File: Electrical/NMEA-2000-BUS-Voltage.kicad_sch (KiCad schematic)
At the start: 6 parts, among them SW1 SW_Push, U1 WeMos_D1_mini

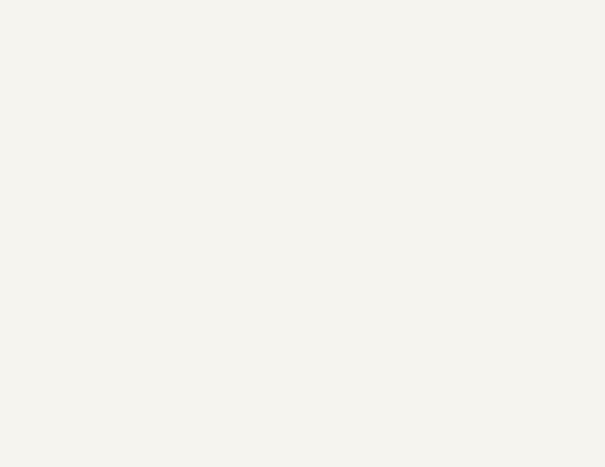
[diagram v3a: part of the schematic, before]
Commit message: Added LM7805
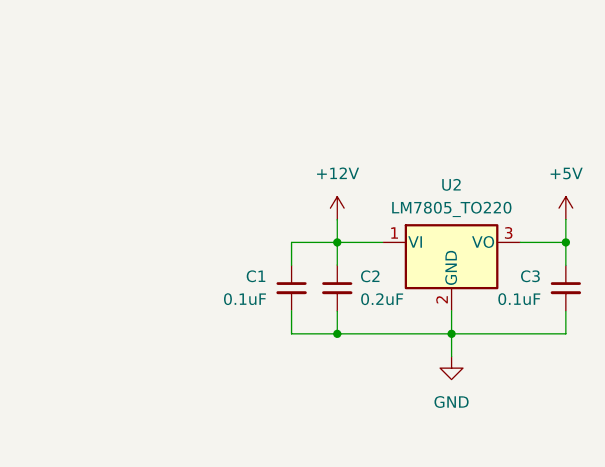
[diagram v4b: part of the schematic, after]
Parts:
- added C1, C3: 0.1uF, symbol Device:C_Small
- added C2: 0.2uF, symbol Device:C_Small
- added U2: LM7805_TO220, Package_TO_SOT_THT:TO-220-3_Vertical, symbol Regulator_Linear:LM7805_TO220
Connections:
- net +12V: now also C1.1, C2.1, U2.1 (VI)
- net +5V: now also C3.1, U2.3 (VO)
- net GND: now also C1.2, C2.2, C3.2, U2.2 (GND)
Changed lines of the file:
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@@
 (kicad_sch (version 20230121) (generator eeschema)
   (paper "A4")
+  (junction (at 168.91 114.3) (diameter 0) (color 0 0 0 0)
+  )
+  (junction (at 181.61 114.3) (diameter 0) (color 0 0 0 0)
+  )
+  (junction (at 168.91 104.14) (diameter 0) (color 0 0 0 0)
+  )
+  (junction (at 194.31 104.14) (diameter 0) (color 0 0 0 0)
+  )
   (junction (at 96.52 80.01) (diameter 0) (color 0 0 0 0)
   )
@@
     (stroke (width 0) (type default))
   )
+  (wire (pts (xy 168.91 101.6) (xy 168.91 104.14))
+    (stroke (width 0) (type default))
+  )
+  (wire (pts (xy 163.83 104.14) (xy 163.83 106.68))
+    (stroke (width 0) (type default))
+  )
+  (wire (pts (xy 168.91 104.14) (xy 163.83 104.14))
+    (stroke (width 0) (type default))
+  )
   (wire (pts (xy 46.99 74.93) (xy 46.99 77.47))
     (stroke (width 0) (type default))
   )
+  (wire (pts (xy 194.31 104.14) (xy 194.31 106.68))
+    (stroke (width 0) (type default))
+  )
   (wire (pts (xy 96.52 110.49) (xy 96.52 113.03))
     (stroke (width 0) (type default))
@@
     (stroke (width 0) (type default))
   )
+  (wire (pts (xy 168.91 114.3) (xy 181.61 114.3))
+    (stroke (width 0) (type default))
+  )
   (wire (pts (xy 64.77 92.71) (xy 59.69 92.71))
     (stroke (width 0) (type default))
@@
     (stroke (width 0) (type default))
   )
+  (wire (pts (xy 168.91 111.76) (xy 168.91 114.3))
+    (stroke (width 0) (type default))
+  )
+  (wire (pts (xy 194.31 114.3) (xy 194.31 111.76))
+    (stroke (width 0) (type default))
+  )
   (wire (pts (xy 59.69 95.25) (xy 64.77 95.25))
     (stroke (width 0) (type default))
@@
     (stroke (width 0) (type default))
   )
+  (wire (pts (xy 181.61 114.3) (xy 194.31 114.3))
+    (stroke (width 0) (type default))
+  )
+  (wire (pts (xy 189.23 104.14) (xy 194.31 104.14))
+    (stroke (width 0) (type default))
+  )
+  (wire (pts (xy 181.61 111.76) (xy 181.61 114.3))
+    (stroke (width 0) (type default))
+  )
+  (wire (pts (xy 168.91 104.14) (xy 173.99 104.14))
+    (stroke (width 0) (type default))
+  )
   (wire (pts (xy 59.69 85.09) (xy 64.77 85.09))
     (stroke (width 0) (type default))
@@
     (stroke (width 0) (type default))
   )
+  (wire (pts (xy 163.83 111.76) (xy 163.83 114.3))
+    (stroke (width 0) (type default))
+  )
   (wire (pts (xy 34.29 95.25) (xy 39.37 95.25))
     (stroke (width 0) (type default))
   )
+  (wire (pts (xy 168.91 104.14) (xy 168.91 106.68))
+    (stroke (width 0) (type default))
+  )
+  (wire (pts (xy 181.61 114.3) (xy 181.61 116.84))
+    (stroke (width 0) (type default))
+  )
   (wire (pts (xy 64.77 107.95) (xy 59.69 107.95))
     (stroke (width 0) (type default))
   )
   (wire (pts (xy 124.46 74.93) (xy 124.46 77.47))
+    (stroke (width 0) (type default))
+  )
+  (wire (pts (xy 194.31 101.6) (xy 194.31 104.14))
+    (stroke (width 0) (type default))
+  )
+  (wire (pts (xy 163.83 114.3) (xy 168.91 114.3))
     (stroke (width 0) (type default))
   )
@@
   (label "D1" (at 64.77 90.17 180) (fields_autoplaced)
     (effects (font (size 1.27 1.27)) (justify right bottom))
+  )
+  (symbol (lib_id "Device:C_Small") (at 163.83 109.22 0) (unit 1)
+    (in_bom yes) (on_board yes) (dnp no)
+    (property "Reference" "C1" (at 158.75 107.95 0)
+      (effects (font (size 1.27 1.27)) (justify left))
+    )
+    (property "Value" "0.1uF" (at 156.21 110.49 0)
+      (effects (font (size 1.27 1.27)) (justify left))
+    )
+    (property "Footprint" "" (at 163.83 109.22 0)
+      (effects (font (size 1.27 1.27)) hide)
+    )
+    (property "Datasheet" "~" (at 163.83 109.22 0)
+      (effects (font (size 1.27 1.27)) hide)
+    )
+    (pin "1")
+    (pin "2")
+    (instances
+      (project "NMEA-2000-BUS-Voltage"
+        (path "/2ad9a196-bb2f-4407-b356-e110a1476183"
+          (reference "C1") (unit 1)
+        )
+      )
+    )
   )
   (symbol (lib_id "MCU_Module:WeMos_D1_mini") (at 49.53 97.79 0) (unit 1)
@@
     )
   )
+  (symbol (lib_id "power:+12V") (at 168.91 101.6 0) (unit 1)
+    (in_bom yes) (on_board yes) (dnp no) (fields_autoplaced)
+    (property "Reference" "#PWR07" (at 168.91 105.41 0)
+      (effects (font (size 1.27 1.27)) hide)
+    )
+    (property "Value" "+12V" (at 168.91 96.52 0)
+      (effects (font (size 1.27 1.27)))
+    )
+    (property "Footprint" "" (at 168.91 101.6 0)
+      (effects (font (size 1.27 1.27)) hide)
+    )
+    (property "Datasheet" "" (at 168.91 101.6 0)
+      (effects (font (size 1.27 1.27)) hide)
+    )
+    (pin "1")
+    (instances
+      (project "NMEA-2000-BUS-Voltage"
+        (path "/2ad9a196-bb2f-4407-b356-e110a1476183"
+          (reference "#PWR07") (unit 1)
+        )
+      )
+    )
+  )
   (symbol (lib_id "power:GND") (at 96.52 113.03 0) (unit 1)
     (in_bom yes) (on_board yes) (dnp no) (fields_autoplaced)
@@
     )
   )
+  (symbol (lib_id "power:GND") (at 181.61 116.84 0) (unit 1)
+    (in_bom yes) (on_board yes) (dnp no) (fields_autoplaced)
+    (property "Reference" "#PWR08" (at 181.61 123.19 0)
+      (effects (font (size 1.27 1.27)) hide)
+    )
+    (property "Value" "GND" (at 181.61 121.92 0)
+      (effects (font (size 1.27 1.27)))
+    )
+    (property "Footprint" "" (at 181.61 116.84 0)
+      (effects (font (size 1.27 1.27)) hide)
+    )
+    (property "Datasheet" "" (at 181.61 116.84 0)
+      (effects (font (size 1.27 1.27)) hide)
+    )
+    (pin "1")
+    (instances
+      (project "NMEA-2000-BUS-Voltage"
+        (path "/2ad9a196-bb2f-4407-b356-e110a1476183"
+          (reference "#PWR08") (unit 1)
+        )
+      )
+    )
+  )
   (symbol (lib_id "power:GND") (at 124.46 77.47 0) (unit 1)
     (in_bom yes) (on_board yes) (dnp no) (fields_autoplaced)
@@
     )
   )
+  (symbol (lib_id "Device:C_Small") (at 194.31 109.22 0) (unit 1)
+    (in_bom yes) (on_board yes) (dnp no)
+    (property "Reference" "C3" (at 189.23 107.95 0)
+      (effects (font (size 1.27 1.27)) (justify left))
+    )
+    (property "Value" "0.1uF" (at 186.69 110.49 0)
+      (effects (font (size 1.27 1.27)) (justify left))
+    )
+    (property "Footprint" "" (at 194.31 109.22 0)
+      (effects (font (size 1.27 1.27)) hide)
+    )
+    (property "Datasheet" "~" (at 194.31 109.22 0)
+      (effects (font (size 1.27 1.27)) hide)
+    )
+    (pin "1")
+    (pin "2")
+    (instances
+      (project "NMEA-2000-BUS-Voltage"
+        (path "/2ad9a196-bb2f-4407-b356-e110a1476183"
+          (reference "C3") (unit 1)
+        )
+      )
+    )
+  )
+  (symbol (lib_id "Device:C_Small") (at 168.91 109.22 0) (unit 1)
+    (in_bom yes) (on_board yes) (dnp no) (fields_autoplaced)
+    (property "Reference" "C2" (at 171.45 107.9563 0)
+      (effects (font (size 1.27 1.27)) (justify left))
+    )
+    (property "Value" "0.2uF" (at 171.45 110.4963 0)
+      (effects (font (size 1.27 1.27)) (justify left))
+    )
+    (property "Footprint" "" (at 168.91 109.22 0)
+      (effects (font (size 1.27 1.27)) hide)
+    )
+    (property "Datasheet" "~" (at 168.91 109.22 0)
+      (effects (font (size 1.27 1.27)) hide)
+    )
+    (pin "1")
+    (pin "2")
+    (instances
+      (project "NMEA-2000-BUS-Voltage"
+        (path "/2ad9a196-bb2f-4407-b356-e110a1476183"
+          (reference "C2") (unit 1)
+        )
+      )
+    )
+  )
   (symbol (lib_id "Device:R") (at 96.52 96.52 0) (unit 1)
     (in_bom yes) (on_board yes) (dnp no) (fields_autoplaced)
@@
     )
   )
+  (symbol (lib_id "power:+5V") (at 194.31 101.6 0) (unit 1)
+    (in_bom yes) (on_board yes) (dnp no) (fields_autoplaced)
+    (property "Reference" "#PWR09" (at 194.31 105.41 0)
+      (effects (font (size 1.27 1.27)) hide)
+    )
+    (property "Value" "+5V" (at 194.31 96.52 0)
+      (effects (font (size 1.27 1.27)))
+    )
+    (property "Footprint" "" (at 194.31 101.6 0)
+      (effects (font (size 1.27 1.27)) hide)
+    )
+    (property "Datasheet" "" (at 194.31 101.6 0)
+      (effects (font (size 1.27 1.27)) hide)
+    )
+    (pin "1")
+    (instances
+      (project "NMEA-2000-BUS-Voltage"
+        (path "/2ad9a196-bb2f-4407-b356-e110a1476183"
+          (reference "#PWR09") (unit 1)
+        )
+      )
+    )
+  )
   (symbol (lib_id "power:+12V") (at 96.52 67.31 0) (unit 1)
     (in_bom yes) (on_board yes) (dnp no) (fields_autoplaced)
@@
         )
       )
+    )
+  )
+  (symbol (lib_id "Regulator_Linear:LM7805_TO220") (at 181.61 104.14 0) (unit 1)
+    (in_bom yes) (on_board yes) (dnp no) (fields_autoplaced)
+    (property "Reference" "U2" (at 181.61 97.79 0)
+      (effects (font (size 1.27 1.27)))
+    )
+    (property "Value" "LM7805_TO220" (at 181.61 100.33 0)
+      (effects (font (size 1.27 1.27)))
+    )
+    (property "Footprint" "Package_TO_SOT_THT:TO-220-3_Vertical" (at 181.61 98.425 0)
+      (effects (font (size 1.27 1.27) italic) hide)
+    )
+    (property "Datasheet" "https://www.onsemi.cn/PowerSolutions/document/MC7800-D.PDF" (at 181.61 105.41 0)
+      (effects (font (size 1.27 1.27)) hide)
+    )
+    (pin "1")
+    (pin "2")
+    (pin "3")
+    (instances
+      (project "NMEA-2000-BUS-Voltage"
+        (path "/2ad9a196-bb2f-4407-b356-e110a1476183"
+          (reference "U2") (unit 1)
+        )
+      )

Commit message: Added Connector
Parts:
- added J1: Conn_01x07, symbol Connector_Generic:Conn_01x07
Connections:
- net +12V: now also J1.1 (Pin_1)
- net +5V: now also J1.2 (Pin_2)
- net D1: now also J1.5 (Pin_5)
- net GND: now also J1.6 (Pin_6), J1.7 (Pin_7)
- net RX: now also J1.3 (Pin_3)
- net TX: now also J1.4 (Pin_4)
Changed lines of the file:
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@@
   (junction (at 168.91 114.3) (diameter 0) (color 0 0 0 0)
+  )
+  (junction (at 215.9 135.89) (diameter 0) (color 0 0 0 0)
   )
   (junction (at 181.61 114.3) (diameter 0) (color 0 0 0 0)
@@
     (stroke (width 0) (type default))
   )
+  (wire (pts (xy 213.36 118.11) (xy 213.36 123.19))
+    (stroke (width 0) (type default))
+  )
+  (wire (pts (xy 220.98 120.65) (xy 215.9 120.65))
+    (stroke (width 0) (type default))
+  )
   (wire (pts (xy 59.69 90.17) (xy 64.77 90.17))
     (stroke (width 0) (type default))
   )
+  (wire (pts (xy 220.98 135.89) (xy 215.9 135.89))
+    (stroke (width 0) (type default))
+  )
   (wire (pts (xy 91.44 80.01) (xy 96.52 80.01))
     (stroke (width 0) (type default))
@@
     (stroke (width 0) (type default))
   )
+  (wire (pts (xy 215.9 135.89) (xy 215.9 138.43))
+    (stroke (width 0) (type default))
+  )
   (wire (pts (xy 52.07 74.93) (xy 52.07 77.47))
     (stroke (width 0) (type default))
@@
     (stroke (width 0) (type default))
   )
+  (wire (pts (xy 215.9 128.27) (xy 220.98 128.27))
+    (stroke (width 0) (type default))
+  )
   (wire (pts (xy 181.61 114.3) (xy 194.31 114.3))
     (stroke (width 0) (type default))
@@
     (stroke (width 0) (type default))
   )
+  (wire (pts (xy 220.98 133.35) (xy 215.9 133.35))
+    (stroke (width 0) (type default))
+  )
+  (wire (pts (xy 220.98 130.81) (xy 215.9 130.81))
+    (stroke (width 0) (type default))
+  )
   (wire (pts (xy 181.61 111.76) (xy 181.61 114.3))
     (stroke (width 0) (type default))
@@
     (stroke (width 0) (type default))
   )
+  (wire (pts (xy 215.9 133.35) (xy 215.9 135.89))
+    (stroke (width 0) (type default))
+  )
+  (wire (pts (xy 215.9 125.73) (xy 220.98 125.73))
+    (stroke (width 0) (type default))
+  )
   (wire (pts (xy 124.46 64.77) (xy 124.46 59.69))
     (stroke (width 0) (type default))
@@
     (stroke (width 0) (type default))
   )
+  (wire (pts (xy 215.9 118.11) (xy 215.9 120.65))
+    (stroke (width 0) (type default))
+  )
   (wire (pts (xy 64.77 107.95) (xy 59.69 107.95))
+    (stroke (width 0) (type default))
+  )
+  (wire (pts (xy 220.98 123.19) (xy 213.36 123.19))
     (stroke (width 0) (type default))
   )
@@
     (effects (font (size 1.27 1.27)) (justify left bottom))
   )
+  (label "D1" (at 215.9 130.81 0) (fields_autoplaced)
+    (effects (font (size 1.27 1.27)) (justify left bottom))
+  )
   (label "FLS" (at 124.46 59.69 270) (fields_autoplaced)
     (effects (font (size 1.27 1.27)) (justify right bottom))
@@
   (label "D1" (at 64.77 90.17 180) (fields_autoplaced)
     (effects (font (size 1.27 1.27)) (justify right bottom))
+  )
+  (label "TX" (at 215.9 128.27 0) (fields_autoplaced)
+    (effects (font (size 1.27 1.27)) (justify left bottom))
+  )
+  (label "RX" (at 215.9 125.73 0) (fields_autoplaced)
+    (effects (font (size 1.27 1.27)) (justify left bottom))
   )
   (symbol (lib_id "Device:C_Small") (at 163.83 109.22 0) (unit 1)
@@
     )
   )
+  (symbol (lib_id "power:+12V") (at 215.9 118.11 0) (unit 1)
+    (in_bom yes) (on_board yes) (dnp no)
+    (property "Reference" "#PWR010" (at 215.9 121.92 0)
+      (effects (font (size 1.27 1.27)) hide)
+    )
+    (property "Value" "+12V" (at 215.9 113.03 90)
+      (effects (font (size 1.27 1.27)))
+    )
+    (property "Footprint" "" (at 215.9 118.11 0)
+      (effects (font (size 1.27 1.27)) hide)
+    )
+    (property "Datasheet" "" (at 215.9 118.11 0)
+      (effects (font (size 1.27 1.27)) hide)
+    )
+    (pin "1")
+    (instances
+      (project "NMEA-2000-BUS-Voltage"
+        (path "/2ad9a196-bb2f-4407-b356-e110a1476183"
+          (reference "#PWR010") (unit 1)
+        )
+      )
+    )
+  )
   (symbol (lib_id "power:GND") (at 96.52 113.03 0) (unit 1)
     (in_bom yes) (on_board yes) (dnp no) (fields_autoplaced)
@@
         (path "/2ad9a196-bb2f-4407-b356-e110a1476183"
           (reference "#PWR01") (unit 1)
+        )
+      )
+    )
+  )
+  (symbol (lib_id "power:GND") (at 215.9 138.43 0) (unit 1)
+    (in_bom yes) (on_board yes) (dnp no) (fields_autoplaced)
+    (property "Reference" "#PWR011" (at 215.9 144.78 0)
+      (effects (font (size 1.27 1.27)) hide)
+    )
+    (property "Value" "GND" (at 215.9 143.51 0)
+      (effects (font (size 1.27 1.27)))
+    )
+    (property "Footprint" "" (at 215.9 138.43 0)
+      (effects (font (size 1.27 1.27)) hide)
+    )
+    (property "Datasheet" "" (at 215.9 138.43 0)
+      (effects (font (size 1.27 1.27)) hide)
+    )
+    (pin "1")
+    (instances
+      (project "NMEA-2000-BUS-Voltage"
+        (path "/2ad9a196-bb2f-4407-b356-e110a1476183"
+          (reference "#PWR011") (unit 1)
         )
       )
@@
         )
       )
+    )
+  )
+  (symbol (lib_id "power:+5V") (at 213.36 118.11 0) (unit 1)
+    (in_bom yes) (on_board yes) (dnp no)
+    (property "Reference" "#PWR012" (at 213.36 121.92 0)
+      (effects (font (size 1.27 1.27)) hide)
+    )
+    (property "Value" "+5V" (at 213.36 113.03 90)
+      (effects (font (size 1.27 1.27)))
+    )
+    (property "Footprint" "" (at 213.36 118.11 0)
+      (effects (font (size 1.27 1.27)) hide)
+    )
+    (property "Datasheet" "" (at 213.36 118.11 0)
+      (effects (font (size 1.27 1.27)) hide)
+    )
+    (pin "1")
+    (instances
+      (project "NMEA-2000-BUS-Voltage"
+        (path "/2ad9a196-bb2f-4407-b356-e110a1476183"
+          (reference "#PWR012") (unit 1)
+        )
+      )
+    )
+  )
+  (symbol (lib_id "Connector_Generic:Conn_01x07") (at 226.06 128.27 0) (unit 1)
+    (in_bom yes) (on_board yes) (dnp no) (fields_autoplaced)
+    (property "Reference" "J1" (at 228.6 127 0)
+      (effects (font (size 1.27 1.27)) (justify left))
+    )
+    (property "Value" "Conn_01x07" (at 228.6 129.54 0)
+      (effects (font (size 1.27 1.27)) (justify left))
+    )
+    (property "Footprint" "" (at 226.06 128.27 0)
+      (effects (font (size 1.27 1.27)) hide)
+    )
+    (property "Datasheet" "~" (at 226.06 128.27 0)
+      (effects (font (size 1.27 1.27)) hide)
+    )
+    (pin "1")
+    (pin "2")
+    (pin "3")
+    (pin "4")
+    (pin "5")
+    (pin "6")
+    (pin "7")
+    (instances
+      (project "NMEA-2000-BUS-Voltage"
+        (path "/2ad9a196-bb2f-4407-b356-e110a1476183"
+          (reference "J1") (unit 1)
+        )
+      )

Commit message: git status
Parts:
- added J2: Conn_01x02, symbol Connector_Generic:Conn_01x02
- added U4: ~, symbol Interface_CAN_LIN:MCP2515_Module
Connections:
- net +5V: now also U4. (VCC)
- net GND: now also U4. (VCC)
- net SCK: now reaches U1.4 (SCK/D5)
- net SCK: now also U4. (VCC)
- net MISO: now reaches U1.5 (MISO/D6)
- net MISO: now also U4. (VCC)
- net MOSI: now reaches U1.6 (MOSI/D7)
- net MOSI: now also U4. (VCC)
- net CS: now reaches U1.7 (CS/D8)
- net CS: now also U4. (VCC)
- new net: J2.1 (Pin_1), U4. (VCC)
- new net: J2.2 (Pin_2), U4. (VCC)
- no-connect marks 8 -> 5
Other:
- moved on the sheet: C1, C2, C3, J1, SW1, U2
